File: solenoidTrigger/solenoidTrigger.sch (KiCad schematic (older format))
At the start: 41 parts, among them J1 Conn_01x20_Female, J2 Conn_02x03_Odd_Even, P1 CONN_02X03, U6 LM3480, Y1 Crystal_SMD

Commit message: After Oct 21 meeting
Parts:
- removed Q? (x2): 2N7000, Package_TO_SOT_THT:TO-92_Inline, symbol Transistor_FET:2N7000
- removed R? (x2): R_100, footprints:R_0805_OEM, symbol Rocketry:R_100
- added Q? (x2): NMOS_CDS16, rocketry:CSD16322Q5, symbol Rocketry:NMOS_CDS16
- added R? (x2): R_1K, footprints:R_0805_OEM, symbol Rocketry:R_1K
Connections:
- wire segments 116 -> 124
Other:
- note added: "transistor"
- note removed: "do these 3 pin connectors follow the ctrl pins or go before them?\n"
- moved on the sheet: C?, R?, U?, Y?

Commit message: As of Oct 30, documented with to do list and questions. When these are resolved, I think we can move on to the next step (probably laying out the actual PCB footprints)
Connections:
- net labels removed: AtmegaToRelay, RadioConnOut, sol_1
- wire segments 124 -> 122
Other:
- note added: "Additional Questions:\n - Should I be using both SCK and SCL on the Atmega? Which one \n should the connectors connect to?\n - Should the Interrupt (IRQ, from radio/solenoid connectors) \n connect to the Atmega? If so, on which port?\n - Should the Chip Select (CS, from radio/solenoid connectors) \n connect to the Atmega? If so, on which port?\n - Do I need an SDA on the Atmega like the example b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"
- note added: "To do:\n - Should the solenoid connector ports be the same as the radio \n connector ones like I did? \n This is just a placeholder right?\n - Update ports on Atmega due to net label changes (fuse, \n transistors, radio, programming?)"
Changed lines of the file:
@@
 Text Label 1700 8350 0    50   ~ 0
 MISO
-Wire Wire Line
-	1700 8050 1950 8050
-Wire Wire Line
-	1950 8050 1950 8100
-$Comp
-L power:GND #PWR?
-U 1 1 5DE0B4B9
-P 1950 8100
-F 0 "#PWR?" H 1950 7850 50  0001 C CNN
-F 1 "GND" H 1955 7927 50  0000 C CNN
-F 2 "" H 1950 8100 50  0001 C CNN
-F 3 "" H 1950 8100 50  0001 C CNN
-	1    1950 8100
-	1    0    0    -1
-$EndComp
 Text Label 1700 8150 0    50   ~ 0
 5V
@@
 Text Label 1650 10200 0    50   ~ 0
 MISO
-Wire Wire Line
-	1650 9900 1900 9900
-Wire Wire Line
-	1900 9900 1900 9950
-$Comp
-L power:GND #PWR?
-U 1 1 5DAF6BDD
-P 1900 9950
-F 0 "#PWR?" H 1900 9700 50  0001 C CNN
-F 1 "GND" H 1905 9777 50  0000 C CNN
-F 2 "" H 1900 9950 50  0001 C CNN
-F 3 "" H 1900 9950 50  0001 C CNN
-	1    1900 9950
-	1    0    0    -1
-$EndComp
 Text Label 1650 10000 0    50   ~ 0
 12V
@@
 	-1   0    0    -1
 $EndComp
-Text Label 8300 8100 2    50   ~ 0
-RadioConnOut
-Text Label 8300 8200 2    50   ~ 0
-12V
-Text Label 8300 8300 2    50   ~ 0
-AtmegaToRelay
-Text Label 8300 8900 2    50   ~ 0
-sol_1
 $Comp
 L solenoidTrigger-rescue:Crystal_SMD-formula Y?
@@
 Text Notes 5050 10200 0    50   ~ 0
 transistor
+Wire Wire Line
+	1700 8050 2000 8050
+$Comp
+L power:GND #PWR?
+U 1 1 5DBB9B5B
+P 2000 8050
+F 0 "#PWR?" H 2000 7800 50  0001 C CNN
+F 1 "GND" H 2005 7877 50  0000 C CNN
+F 2 "" H 2000 8050 50  0001 C CNN
+F 3 "" H 2000 8050 50  0001 C CNN
+	1    2000 8050
+	1    0    0    -1
+$EndComp
+Wire Wire Line
+	1650 9900 1950 9900
+$Comp
+L power:GND #PWR?
+U 1 1 5DBC43FE
+P 1950 9900
+F 0 "#PWR?" H 1950 9650 50  0001 C CNN
+F 1 "GND" H 1955 9727 50  0000 C CNN
+F 2 "" H 1950 9900 50  0001 C CNN
+F 3 "" H 1950 9900 50  0001 C CNN
+	1    1950 9900
+	1    0    0    -1
+$EndComp
+Text Notes 9950 6850 0    98   ~ 0
+To do:\n   - Should the solenoid connector ports be the same as the radio \n      connector ones like I did? \n      This is just a placeholder right?\n   - Update ports on Atmega due to net label changes (fuse, \n      transistors, radio, programming?)
+Text Notes 9950 9300 0    98   ~ 0
+Additional Questions:\n   - Should I be using both SCK and SCL on the Atmega? Which one \n     should the connectors connect to?\n   - Should the Interrupt (IRQ, from radio/solenoid connectors) \n     connect to the Atmega? If so, on which port?\n   - Should the Chip Select (CS, from radio/solenoid connectors) \n     connect to the Atmega? If so, on which port?\n   - Do I need an SDA on the Atmega like the example board has?\n   - Do the net labels work as intended, or do they not connect in the \n     correct order right now with how I have it set up?\n   - Is there only one reset crystal on the entire PCB (on the Atmega)\n     that all resets of the connectors connect to or should I add a reset \n     crystal for each connector that has a reset port?\n   - Are all connectors connected to Atmega along one MISO/MOSI/5V/\n     SCLK line, or shold I have separate lines for each connector?\n   - No AREF right? (example Atmega above doesn't have one)
 $EndSCHEMATC

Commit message: As of Nov 1, started adding LEDs
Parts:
- removed J?: Solenoid Connector, footprints:micromatch_female_ra_10, symbol solenoidTrigger-rescue:MM_F_RA_10-Rocketry
- added D? (x5): LED_0805, footprints:LED_0805_OEM, symbol Rocketry:LED_0805
- added J?: CONN_01X03, Pin_Headers:Pin_Header_Straight_1x03_Pitch2.54mm, symbol Rocketry:CONN_01X03
- added R?: R_499, footprints:R_0805_OEM, symbol Rocketry:R_499
- added R? (x4): R_200, footprints:R_0805_OEM, symbol Rocketry:R_200
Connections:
- net labels added: solenoid_connectors
- net labels removed: SCLK
- wire segments 122 -> 142
- no-connect marks 2 -> 5
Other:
- note added: "Check:\n - Do the net labels work as intended, or do they not connect in the \n correct order right now with how I have it set up?\n"
- note added: "To do:\n - PROGRAMMING LEDS - Done, check resistor values\n - POWER LEDS (1 for 12V, 1 for 5V) - need to do, \n see pic on phone, 2 transistors & 2 control pins \n for each solenoid, of which there are 3\n"
- note removed: "Additional Questions:\n - Should I be using both SCK and SCL on the Atmega? Which one \n should the connectors connect to?\n - Should the Interrupt (IRQ, from radio/solenoid connectors) \n connect to the Atmega? If so, on which port?\n - Should the Chip Select (CS, from radio/solenoid connectors) \n connect to the Atmega? If so, on which port?\n - Do I need an SDA on the Atmega like the example b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"
- note removed: "To do:\n - Should the solenoid connector ports be the same as the radio \n connector ones like I did? \n This is just a placeholder right?\n - Update ports on Atmega due to net label changes (fuse, \n transistors, radio, programming?)"
- moved on the sheet: J?, R?, U?

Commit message: As of Nov 8, PCB schematic almost done
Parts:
- removed D? (x5): LED_0805, footprints:LED_0805_OEM, symbol Rocketry:LED_0805
- removed R?: R_499, footprints:R_0805_OEM, symbol Rocketry:R_499
- removed R? (x4): R_200, footprints:R_0805_OEM, symbol Rocketry:R_200
- added C?: C_0.33uF, footprints:C_0805_OEM, symbol Rocketry:C_0.33uF
- added D? (x5): LED_0805, footprints:LED_0805_OEM, symbol Rocketry:LED_0805
- added Q? (x4): NMOS_CDS16, rocketry:CSD16322Q5, symbol Rocketry:NMOS_CDS16
- added R? (x4): R_200, footprints:R_0805_OEM, symbol Rocketry:R_200
- added R?: R_499, footprints:R_0805_OEM, symbol Rocketry:R_499
- added R? (x4): R_1K, footprints:R_0805_OEM, symbol Rocketry:R_1K
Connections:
- net labels added: 12V_Solenoid1, 12V_Solenoid2, 12V_Solenoid3, PLED1, PLED2, PLED3, ctrl_pin_1-1, ctrl_pin_1-2, ctrl_pin_2-1, ctrl_pin_2-2, ctrl_pin_3-1, ctrl_pin_3-2
- net labels removed: 12V_Solenoid, ctrl_pin
- wire segments 142 -> 155
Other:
- note added: "LEDs"
- note added: "To do:\n - PROGRAMMING LEDS - Done, check resistor values\n - POWER LEDS (1 for 12V, 1 for 5V) - need to do, \n see pic on phone, 2 transistors & 2 control pins \n for each solenoid, of which there are 3\n - solenoid connectors follow transistors\n"
- note removed: "To do:\n - PROGRAMMING LEDS - Done, check resistor values\n - POWER LEDS (1 for 12V, 1 for 5V) - need to do, \n see pic on phone, 2 transistors & 2 control pins \n for each solenoid, of which there are 3\n"
- moved on the sheet: C?, D1, J?, Q?, R14, R?, U?, Y?

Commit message: post-design review 11/15
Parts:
- removed D1: LED_0805, footprints:LED_0805_OEM, symbol solenoidTrigger-rescue:LED_0805-formula
- removed R14: R_200, footprints:R_0805_OEM, symbol solenoidTrigger-rescue:R_200-formula
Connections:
- net labels removed: programming, solenoid_connectors
- wire segments 155 -> 151
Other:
- note added: "programming"
- note added: "solenoid connectors"
- moved on the sheet: C?, D?, F?, J?, Q?, R?, U?

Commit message: Almost ready to start actual layout and traces
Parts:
- removed C1, C10, C7, C9: C_0.1uF, footprints:C_0805_OEM, symbol solenoidTrigger-rescue:C_0.1uF-formula
- removed C2, C3: C_30pF, footprints:C_0805_OEM, symbol solenoidTrigger-rescue:C_30pF-formula
- removed C4: C_100pF, footprints:C_0805_OEM, symbol solenoidTrigger-rescue:C_100pF-formula
- removed D2: LED_0805, footprints:LED_0805_OEM, symbol solenoidTrigger-rescue:LED_0805-formula
- removed F1: Fuse_1A, footprints:R_0805_OEM, symbol Device:Fuse
- removed J1: Conn_01x20_Female, footprints:Pin_Header_Straight_2x10, symbol Connector:Conn_01x20_Female
- removed J2: Conn_02x03_Odd_Even, footprints:Pin_Header_Straight_2x03, symbol Connector_Generic:Conn_02x03_Odd_Even
- removed P1: CONN_02X03, footprints:Pin_Header_Straight_2x03, symbol circuit-rescue:CONN_02X03-formula
- removed R15, R3: R_200, footprints:R_0805_OEM, symbol solenoidTrigger-rescue:R_200-formula
- removed R28: R_100, footprints:R_0805_OEM, symbol solenoidTrigger-rescue:R_100-formula
- removed R?: R_10K, footprints:R_0805_OEM, symbol solenoidTrigger-rescue:R_10K-rocketry
- removed U6: LM3480, TO_SOT_Packages_SMD:SOT-23, symbol solenoidTrigger-rescue:LM3480-formula
- removed U?: ATmega328P-AU, Package_QFP:TQFP-32_7x7mm_P0.8mm, symbol MCU_Microchip_ATmega:ATmega328P-AU
- removed Y1: Crystal_SMD, footprints:Crystal_SMD_FA238, symbol solenoidTrigger-rescue:Crystal_SMD-formula
- added C13: C_0.1uF, footprints:C_0805_OEM, symbol Rocketry:C_0.1uF
- Q1, Q2, Q3, Q4, Q5, Q6: renamed from Q?; footprint rocketry:CSD16322Q5 -> footprints:CSD16322Q5
- gave numbers to parts that had none: 33
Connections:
- net labels removed: 3.3V, SCL, SDA, battery+, battery-, blue_1, blue_2, blue_3, blue_4, blue_5, blue_6, blue_7, blue_8, blue_outA, blue_outB, issues, led_D1, motorA+, motorA-, motorA_DIR, motorA_PWM, motorB+, motorB-, motorB_DIR, motorB_PWM, p_led, red_1, red_2, red_3, red_4, red_5, red_6, red_7, red_8, red_outA, red_outB, select_0A, select_0B, select_1A, select_1B
- wire segments 151 -> 93
- no-connect marks 5 -> 11
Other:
- note added: "Check that no connects are correct\n\nChange library of:\n- fuse\n- solenoid connectors"
- note removed: "LEDS\n"
- note removed: "MAIN"
- note removed: "PINOUT"
- note removed: "POWER"
- note removed: "POWER REGULATORS\n"
- note removed: "PROGRAMMING\n"
- note removed: "SUPPORTING IMAGES"
- moved on the sheet: C5, F2, J4, R8, U1

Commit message: Updated with no errors
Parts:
- added U3: ADG417BN, Package_DIP:DIP-8_W7.62mm, symbol Analog_Switch:ADG417BN
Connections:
- net 12V: now also U3.1; no longer Q1.5 (D), Q1.6 (D), Q1.7 (D), Q1.8 (D), Q2.5 (D), Q2.6 (D), Q2.7 (D), Q2.8 (D), Q3.5 (D), Q3.6 (D), Q3.7 (D), Q3.8 (D), Q4.5 (D), Q4.6 (D), Q4.7 (D), Q4.8 (D), Q5.5 (D), Q5.6 (D), Q5.7 (D), Q5.8 (D), Q6.5 (D), Q6.6 (D), Q6.7 (D), Q6.8 (D)
- new net 12V_Switch: Q1.5 (D), Q1.6 (D), Q1.7 (D), Q1.8 (D), Q2.5 (D), Q2.6 (D), Q2.7 (D), Q2.8 (D), Q3.5 (D), Q3.6 (D), Q3.7 (D), Q3.8 (D), Q4.5 (D), Q4.6 (D), Q4.7 (D), Q4.8 (D), Q5.5 (D), Q5.6 (D), Q5.7 (D), Q5.8 (D), Q6.5 (D), Q6.6 (D), Q6.7 (D), Q6.8 (D), U3.8
- no-connect marks 11 -> 12
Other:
- moved on the sheet: C11, C12, C6, C8, R8, R9, U2, Y2

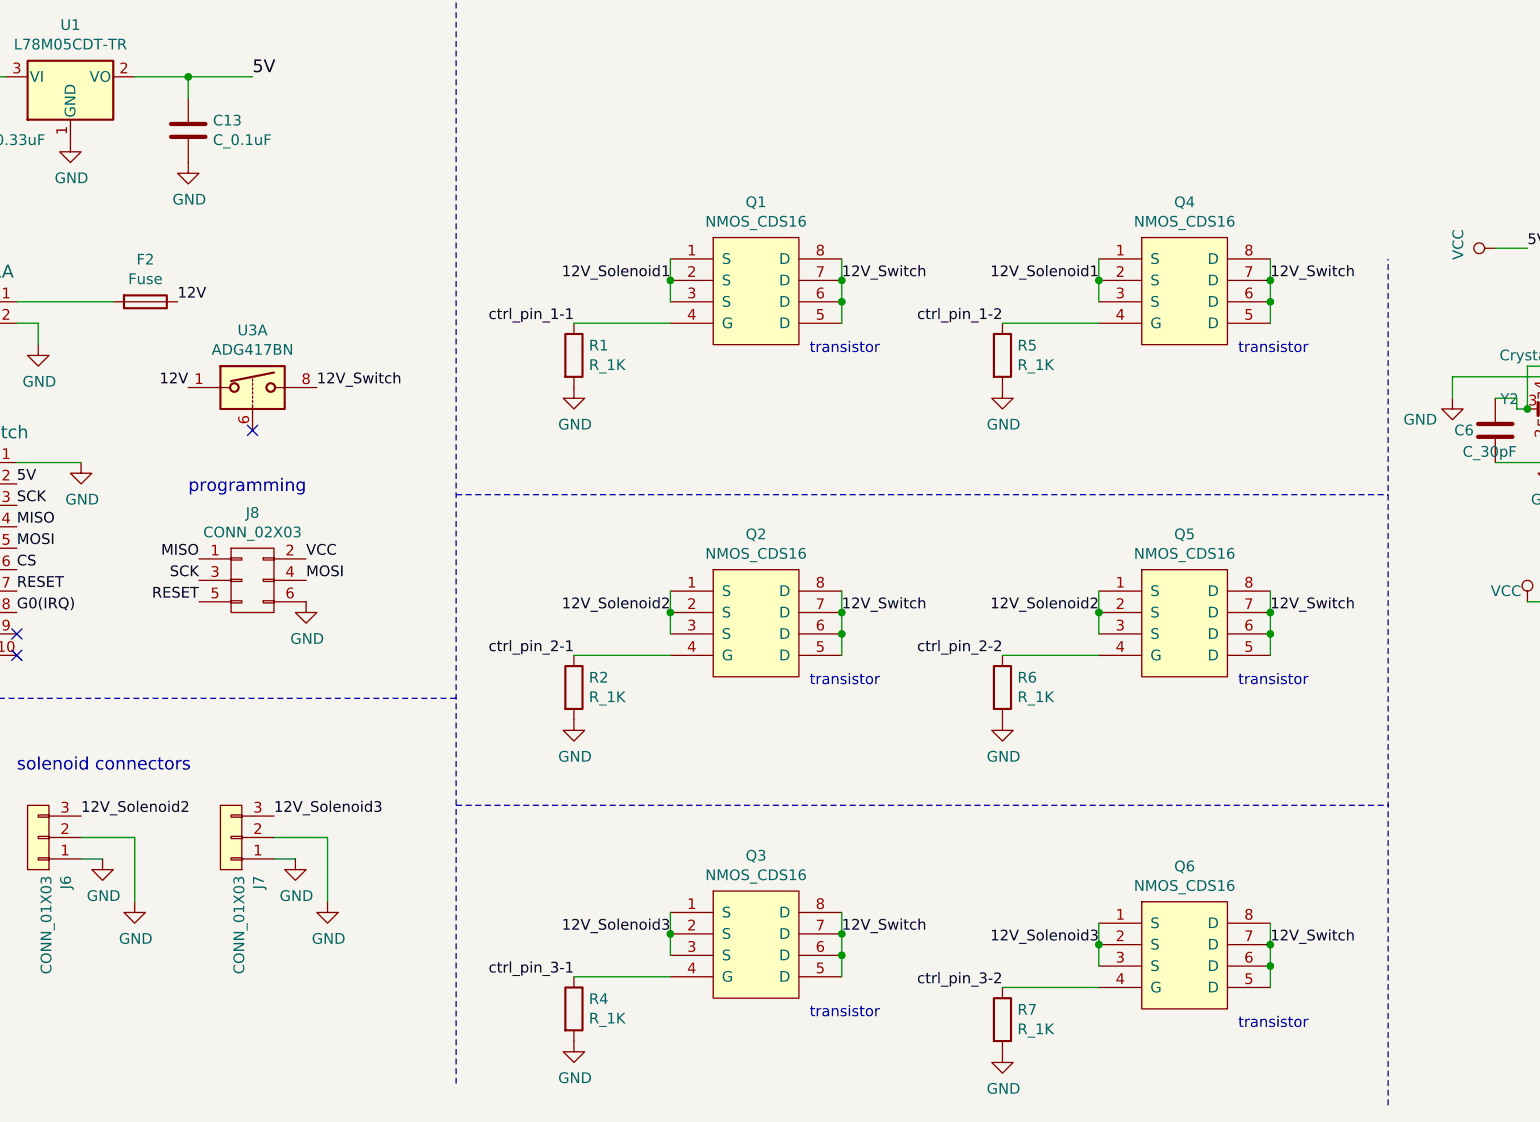
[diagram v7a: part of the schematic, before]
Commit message: Nov 28, have reduced trace overlaps
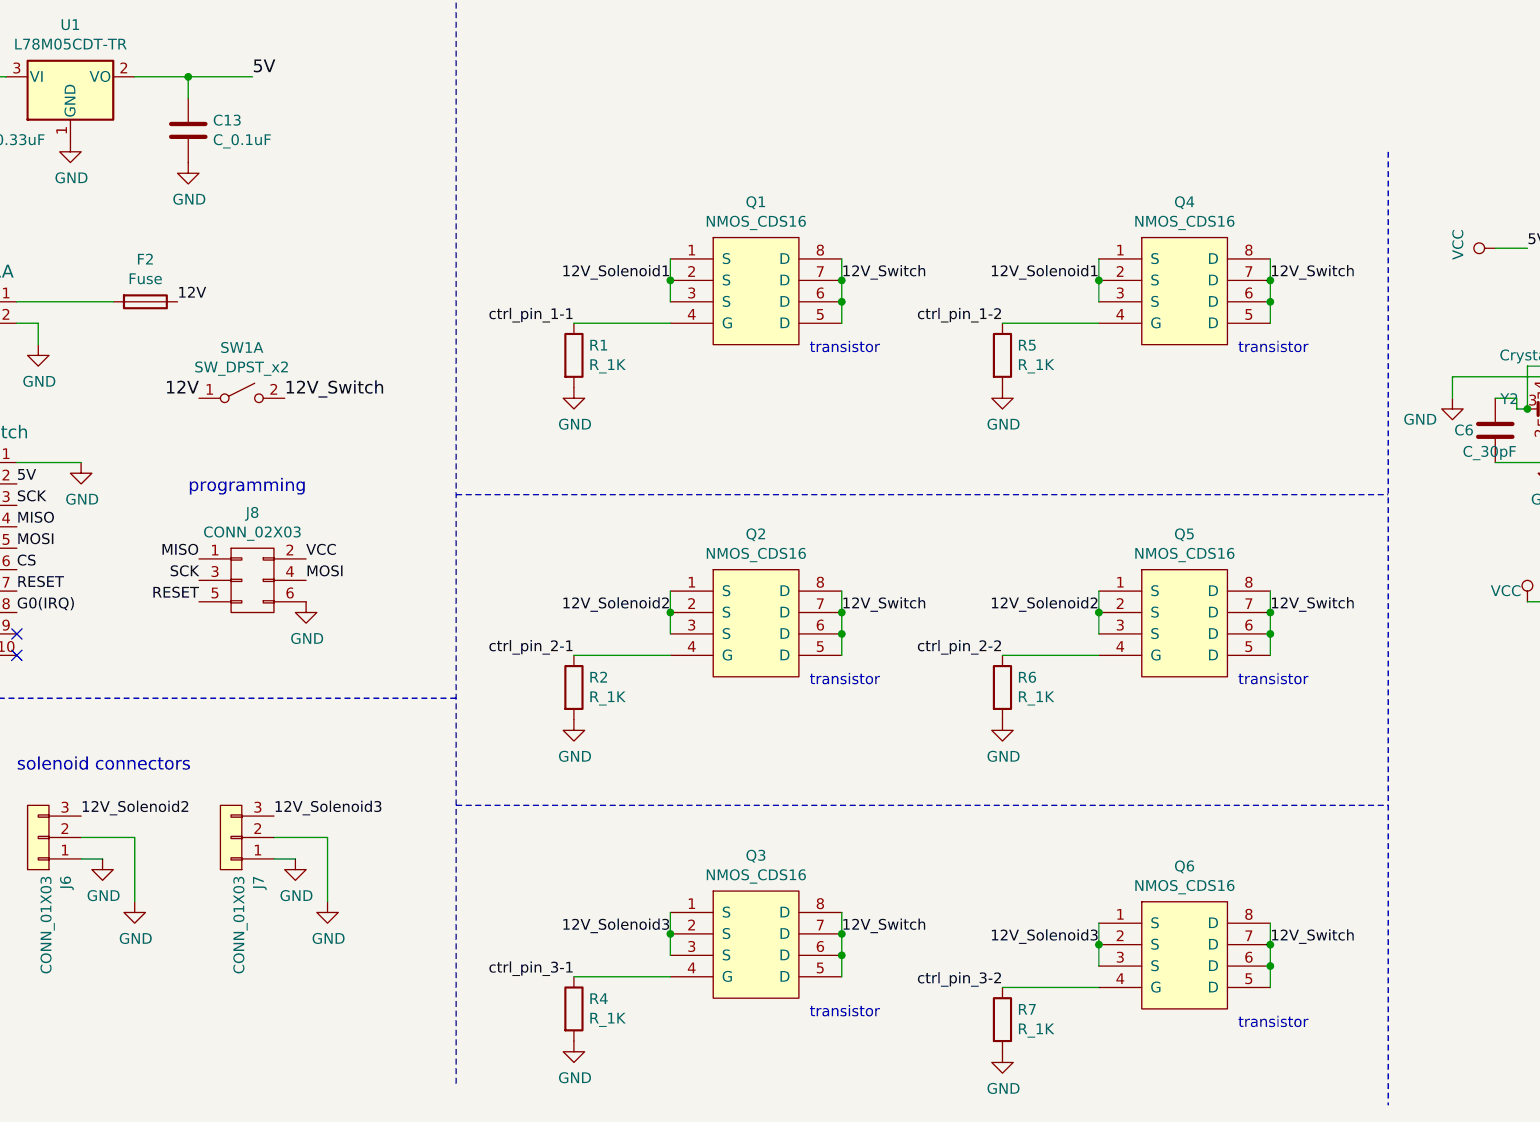
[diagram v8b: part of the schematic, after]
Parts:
- removed U3: ADG417BN, Package_DIP:DIP-8_W7.62mm, symbol Analog_Switch:ADG417BN
- added SW1: SW_DPST_x2, symbol Switch:SW_DPST_x2
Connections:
- net 12V: now also SW1.1 (A)
- net 12V_Switch: now also SW1.2 (B)
- no-connect marks 12 -> 11
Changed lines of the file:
@@
 ctrl_pin_2-1
-Wire Notes Line
-	7950 11100 7950 7150
 Wire Notes Line
 	3600 9200 700  9200
@@
 Text Label 950  6300 2    50   ~ 0
 12V
-Wire Notes Line
-	3600 5550 3600 11000
 Text Notes 1200 5750 0    118  ~ 0
 CONNECTORS
@@
 NoConn ~ 1550 8900
 NoConn ~ 1550 9000
-$Comp
-L Analog_Switch:ADG417BN U3
-U 1 1 5DDA1208
-P 2650 7750
-F 0 "U3" H 2650 8017 50  0000 C CNN
-F 1 "ADG417BN" H 2650 7926 50  0000 C CNN
-F 2 "Package_DIP:DIP-8_W7.62mm" H 2650 7650 50  0001 C CNN
-F 3 "https://www.analog.com/media/en/technical-documentation/data-sheets/ADG417.pdf" H 2650 7750 50  0001 C CNN
-	1    2650 7750
-	1    0    0    -1
-$EndComp
-Text Label 2350 7750 2    50   ~ 0
-12V
-Text Label 2950 7750 0    50   ~ 0
-12V_Switch
 Text Label 5400 7250 0    50   ~ 0
 12V_Switch
@@
 Wire Notes Line
 	3600 9700 7950 9700
-NoConn ~ 2650 7950
+$Comp
+L Switch:SW_DPST_x2 SW1
+U 1 1 5DE0F544
+P 2600 7800
+F 0 "SW1" H 2600 8035 50  0000 C CNN
+F 1 "SW_DPST_x2" H 2600 7944 50  0000 C CNN
+F 2 "" H 2600 7800 50  0001 C CNN
+F 3 "~" H 2600 7800 50  0001 C CNN
+	1    2600 7800
+	1    0    0    -1
+$EndComp
+Text Label 2400 7800 2    59   ~ 0
+12V
+Text Label 2800 7800 0    59   ~ 0
+12V_Switch
+Wire Notes Line
+	7950 6650 7950 11100
+Wire Notes Line
+	3600 5550 3600 11000
 $EndSCHEMATC
